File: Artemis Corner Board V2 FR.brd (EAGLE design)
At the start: 132.4 x 63.1 mm, 68 parts, among them U1 TPS562219, U2 TM4C1231C3PM, U21 LM1085IS, U3 TPS562219, U4 MCP2562FD, Y1 NX3225GA

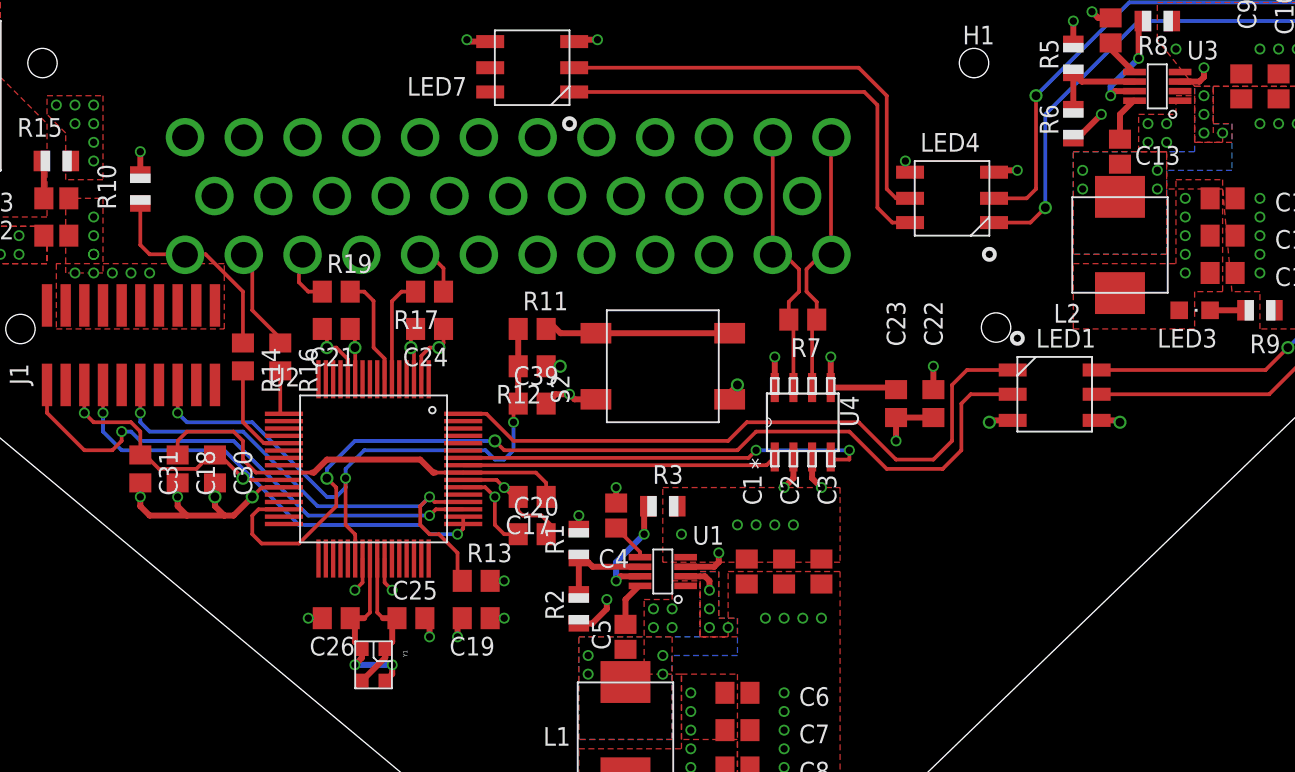
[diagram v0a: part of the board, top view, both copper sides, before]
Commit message: fixed board errors and added ESD Protection
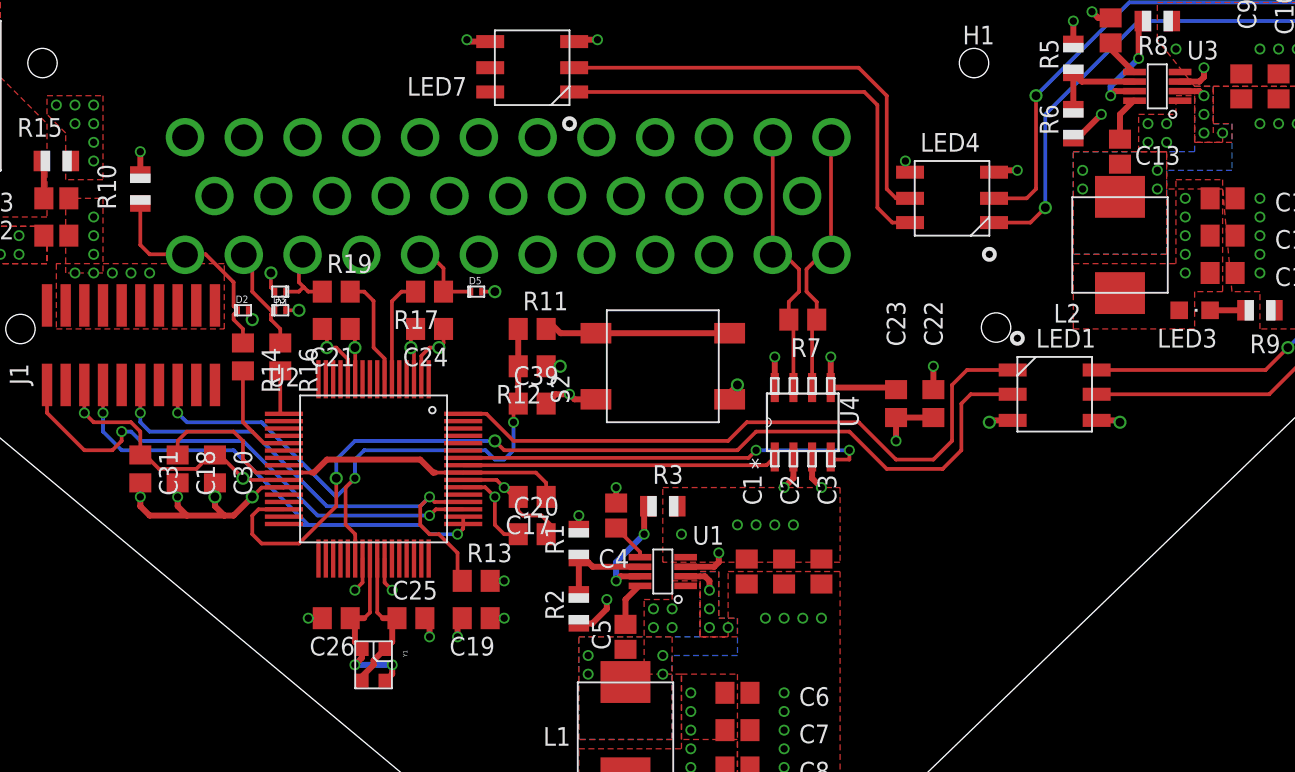
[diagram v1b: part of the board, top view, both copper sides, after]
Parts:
- added D2, D3, D4, D5: TPD1E05U06, FormE:X2SON
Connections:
- net DAMPER_POS_OUT: now also D3.I/O
- net GND: now also D2.GND, D3.GND, D4.GND, D5.GND
- net STRAIN_GADGE_VOLTMETER_IN_0: now also D5.I/O
- net STRAIN_GADGE_VOLTMETER_IN_1: now also D4.I/O
- net WHEEL_SPEED_OUT: now also D2.I/O
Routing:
- net GND: track 71.7 -> 75.7 mm, vias 67 -> 70
- net STRAIN_GADGE_VOLTMETER_IN_0: track 3.59 -> 5.47 mm
- net SW_5V2: track 0.00 -> 1.75 mm
- net STRAIN_GADGE_VOLTMETER_IN_1: track 3.83 -> 5.20 mm
- net TDO: track 31.6 -> 32.2 mm
- net SPI_SCARY_LED_CLOCK: track 66.7 -> 66.2 mm

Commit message: Made list fixes
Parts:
- moved D5 0.63 mm to (7.62, -5.08)
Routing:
- net STRAIN_GADGE_VOLTMETER_IN_0: track 5.47 -> 6.10 mm

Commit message: Updated a lot of stuff
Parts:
- added C62: 4.7uF, rcl:C0805
- added C63: 0.1uF, rcl:C0805
- added FB3: 220R @ 100M, launchpad:0805
- added R20: 2K, rcl:R0805
- C31: value 20uF -> 22uF
- turned C19 to 0 degrees
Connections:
- net P$40 renamed VDDC
- net PROGRAMMING_CAN_N renamed CAN_N
- net PROGRAMMING_CAN_P renamed CAN_P
- net PROGRAMMING_CAN_RX renamed CAN_RX
- net PROGRAMMING_CAN_TX renamed CAN_TX
- new net FILTERED_+3V3: C19.1, C20.1, C21.1, C24.1, C30.1, C31.1, C62.1, C63.1, FB3.2, U2.11, U2.2, U2.26, U2.42, U2.54
- new net N$7: R20.2, U2.41
- net +3V3: now also FB3.1; no longer C19.1, C20.1, C21.1, C24.1, C30.1, C31.1, U2.11, U2.2, U2.26, U2.42, U2.54
- net GND: now also C62.2, C63.2, U2.32, U2.35
- net N$5: now also R20.1; no longer U2.41
- net TDI: now also U2.50
- net TDO: no longer U2.50
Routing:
- net FILTERED_+3V3: track 0.00 -> 34.4 mm, vias 0 -> 6
- net +3V3: track 46.1 -> 14.7 mm, vias 15 -> 9
- net CAN_TX: track 21.7 -> 1.05 mm
- net CAN_RX: track 28.5 -> 9.06 mm
- net N$6: track 12.6 -> 16.6 mm
- net CAN_P: track 18.7 -> 17.5 mm
- net CAN_N: track 18.6 -> 17.3 mm
- net N$5: track 10.3 -> 9.42 mm
- net TDO: track 32.2 -> 31.7 mm

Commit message: Changed to Tiva C with two CAN modules; modified sensor input scaling
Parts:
- removed C62: 4.7uF, rcl:C0805
- removed C63: 0.1uF, rcl:C0805
- removed C72, C73: 10uF, adafruit:C0805
- removed D4, D5: TPD1E05U06, FormE:X2SON
- removed FB3: 220R @ 100M, launchpad:0805
- removed LED5, LED6: GREEN, FormE:CHIPLED_0805
- removed LED7: APA102C, FormE:5050_LED
- removed S2: TE-FSM4JSMATR, FormE:TE-FSM4JSMATR
- removed U21: LM1085IS, FormE:TO-263
- added C27, C33, C34, C35: 0.1uF, rcl:C0805
- added C28: 0.01uF, rcl:C0805
- added C29: 1uF, rcl:C0805
- added C32: 4.7uF, rcl:C0805
- added C36, C42: 0.1uF, adafruit:C0805
- added C37, C38: 10uF, adafruit:C0805
- added C40: 2.2uF, rcl:C0805
- added C41: 8200pF, adafruit:C0805
- added C43, C44: 22uF, rcl:C1210K
- added C45, C46, C47: 22uF, adafruit:C0805
- added CF1, CF2, CF3, CF4: NFM21C, murata-filter:NFM21C
- added D1: TPD1E05U06, FormE:X2SON
- added IC1: FT232RL, ftdichip:SSOP28
- added JP1: (no value), pinhead:1X02
- added JP2: (no value), FormE:MOLEX-MICROUSB-B-105017-0001
- added L3: 4.7uH, FormE:SRP6540
- added Q1: BSS138, FormE:BSS138
- added R21: 1k, adafruit:R0805
- added R22: 54.9k, adafruit:R0805
- added R23: 10K, adafruit:R0805
- added R24: 1K, adafruit:R0805
- added S1: TE-FSM4JSMATR, FormE:TE-FSM4JSMATR
- added U5: MCP2562, FormE:SOIC8-N_MC
- added U6: TPS62177, FormE:TPS6217X
- added U7: TPS62175, FormE:TPS6217X
- added U8: TPS562219, FormE:TPS562219
- added Y2: 32.768kHz, FormE:AB26TRQ
- C1: value 0.1uF -> 100uF; device adafruit:C0805 -> rcl:D/7343-31W
- C10, C2: value 10uF -> 0.1uF; device adafruit:C0805 -> rcl:C0805
- C11: value 10uF -> 2.2uF; device adafruit:C0805 -> rcl:C0805
- C12: value 8200pF -> 2.2uF; device adafruit:C0805 -> rcl:C0805
- C13, C5: device adafruit:C0805 -> rcl:C0805
- C14, C16: value 22uF -> 0.1uF; device adafruit:C0805 -> rcl:C0805
- C15: value 22uF -> DNP/0.1uF; device adafruit:C0805 -> rcl:C0805
- C18: value 3.3uF -> 22pF
- C19: value 0.1uF -> 1uF
- C20, C22, C23: value 0.1uF -> 22pF
- C21: value 0.1uF -> 2.2uF
- C24: value 0.1uF -> 0.01uF
- C25: value 12pF -> 0.1uF
- C26: value 12pF -> 0.01uF
- C3: value 10uF -> 100pF; device adafruit:C0805 -> rcl:C0805
- C31: value 22uF -> 0.1uF
- C39: value 1uF -> 2.2uF
- C4: value 8200pF -> 100pF; device adafruit:C0805 -> rcl:C0805
- C6, C7, C8: value 22uF -> 2.2uF; device adafruit:C0805 -> rcl:C0805
- C9: value 0.1uF -> DNP; device adafruit:C0805 -> rcl:C0805
- D3: value TPD1E05U06 -> MM3Z3V3T1G; device FormE:X2SON -> FormE:SOD-323
- L1, L2: value 4.7uH -> 10uH
- LED1, LED2: value APA102C -> ORANGE; device FormE:5050_LED -> FormE:CHIP-LED0805
- LED3: device FormE:CHIPLED_0805 -> FormE:CHIP-LED0805
- LED4: value APA102C -> GREEN; device FormE:5050_LED -> FormE:CHIP-LED0805
- R1: value 33.2K -> 100R; device adafruit:R0805 -> rcl:R0805
- R10: value 10K -> 270; device adafruit:R0805 -> rcl:R0805
- R11: value 100 -> 120R
- R12: value 2.2K -> 100R
- R13: value 1K -> 10k
- R14: value 22 -> 120R
- R15: value 0.007 -> 270; device adafruit:R0805 -> rcl:R0805
- R16: value 22 -> 270
- R17: value 22 -> 10k
- R18: value 1K -> 4.7k; device adafruit:R0805 -> rcl:R0805
- R19: value 22 -> 75k
- R2: value 10K -> 100R; device adafruit:R0805 -> rcl:R0805
- R20: value 2K -> 150k
- R3: value 10K -> 22; device adafruit:R0805 -> rcl:R0805
- R4: value 1K -> 22; device adafruit:R0805 -> rcl:R0805
- R5: value 33.2K -> 10k; device adafruit:R0805 -> rcl:R0805
- R6: value 10K -> 10k; device adafruit:R0805 -> rcl:R0805
- R7: value 120/DNP -> 10k
- R8: value 10K -> 39k; device adafruit:R0805 -> rcl:R0805
- R9: value 1K -> 75k; device adafruit:R0805 -> rcl:R0805
- U1: value TPS562219 -> OPA365AIDBVR; device FormE:TPS562219 -> FormE:SOT23-5
- U2: value TM4C1231C3PM -> ADS1232IPWR; device FormE:TM4C1231C3PM -> FormE:ADS1232IPW
- U3: value TPS562219 -> MCP2562; device FormE:TPS562219 -> FormE:SOIC8-N_MC
- U4: value MCP2562FD -> TM4C123GH6PMI; device FormE:SOIC8-N_MC -> FormE:PQFP-64
- Y1: value NX3225GA -> 16MHz; device FormE:4-SMD -> FormE:CSM-3X
- moved C23 467.3 mm to (-108.6, -457.2), turned to 0 degrees
- moved C22 462.1 mm to (-108.6, -450.9), turned to 0 degrees
- moved R7 451.0 mm to (-96.5, -440.1), turned to 0 degrees
- moved U1 435.3 mm to (-106.7, -440.7), turned to 0 degrees
- moved C1 412.4 mm to (-93.3, -419.1), turned to 0 degrees
- moved C4 407.2 mm to (-96.5, -411.5), turned to 0 degrees
- moved C3 401.6 mm to (-96.5, -405.1), turned to 0 degrees
- moved C2 394.8 mm to (-96.5, -398.8), turned to 0 degrees
- moved C10 381.1 mm to (-96.5, -337.8), turned to 0 degrees
- moved C12 374.1 mm to (-96.5, -331.5), turned to 0 degrees
- moved C11 370.6 mm to (-96.5, -325.1), turned to 0 degrees
- moved C7 363.1 mm to (-96.5, -377.2)
- moved C8 354.8 mm to (-96.5, -370.8)
- moved C6 353.6 mm to (-96.5, -364.5)
- moved R2 349.4 mm to (-96.5, -358.1), turned to 0 degrees
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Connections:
- removed net +12V: H1.1, H1.2, H1.3, LED6.A, R10.2, R15.2
- removed net 12V_CURRENT_SENSE+: C73.1, R15.1, U21.2, U21.GND, U21.GND1
- removed net CAN_N: H1.12, H1.35, R7.1, U4.6
- removed net CAN_P: H1.11, H1.34, R7.2, U4.7
- removed net CAN_RX: U2.58, U4.4
- removed net CAN_TX: U2.57, U4.1
- removed net DAMPER_POS_OUT: D3.I/O, H1.25, R16.1
- removed net DAMPER_POS_OUT_TR: R16.2, U2.17
- removed net FILTERED_+3V3: C19.1, C20.1, C21.1, C24.1, C30.1, C31.1, C62.1, C63.1, FB3.2, U2.11, U2.2, U2.26, U2.42, U2.54
- removed net MCU_RESET: C39.1, J1.15, R11.1, R12.2, U2.38
- removed net N$11: LED6.C, R18.2
- removed net SPI_SCARY_LED_CLOCK: LED1.2, U2.30
- removed net SPI_SCARY_LED_TRANSMIT: LED1.1, U2.64
- removed net SS_5V1: C4.1, U1.5
- removed net SS_5V2: C12.1, U3.5
- removed net STRAIN_GADGE_VOLTMETER_IN_0: D5.I/O, H1.28, R17.1
- removed net STRAIN_GADGE_VOLTMETER_IN_0_TR: R17.2, U2.6
- removed net STRAIN_GADGE_VOLTMETER_IN_1: D4.I/O, H1.26, R19.1
- removed net STRAIN_GADGE_VOLTMETER_IN_1_TR: R19.2, U2.7
- removed net SW_5V1: C5.2, L1.P$1, U1.2
- removed net SW_5V2: C13.2, L2.P$1, U3.2
- removed net TRCLK: U2.31
- removed net VBST_5V1: C5.1, U1.8
- removed net VBST_5V2: C13.1, U3.8
- removed net VDDC: C17.1, C18.1, U2.25, U2.56
- removed net VFB_5V1: R1.1, R2.2, U1.6
- removed net VFB_5V2: R5.1, R6.2, U3.6
- removed net WHEEL_SPEED_OUT: D2.I/O, H1.24, R10.1, R14.1
- removed net WHEEL_SPEED_OUT_TR: R14.2, U2.21
- new net !RESET!: C15.1, J1.15, R12.2, R13.2, U4.38
- new net +1V2: C44.1, L2.P$2, R19.2, U7.10, U7.8, U7.MASK-10, U7.MASK-8
- new net ADC_!PWDN!: U2.22, U4.46
- new net ADC_CHANNEL_SELECT: U2.8, U4.48
- new net ADC_GAIN_BIT_0: U2.19, U4.58
- new net ADC_GAIN_BIT_1: U2.20, U4.57
- new net ADC_MISO: U2.24, U4.21
- new net ADC_SCLK: U2.23, U4.19
- new net ADC_SPEED: U2.21, U4.45
- new net ADC_TEMP_EN: U2.7, U4.47
- new net CAR_CAN_N: H1.35, R14.1, U5.6
- new net CAR_CAN_P: H1.34, R14.2, U5.7
- new net CAR_CAN_RX: U4.59, U5.4
- new net CAR_CAN_TX: U4.60, U5.1
- new net DAMPER_POSITION: D1.I/O, H1.25, R3.1
- new net DAMPER_POSITION_3V3: D3.CATHODE, R10.2, U4.6
- new net FB_1V2: R19.1, R20.2, U7.5, U7.MASK-5
- new net IR_SENSOR_CAN_N: H1.12, R11.1, U3.6
- new net IR_SENSOR_CAN_P: H1.11, R11.2, U3.7
- new net N$14: R8.2, U1.1, U1.4
- new net N$17: C23.1, U4.34, Y2.1
- new net N$19: JP1.2, U2.14
- new net N$20: R3.2, R5.1, U1.3
- new net N$21: Q1.D, R4.2, R6.1
- new net N$22: C35.1, IC1.17
- new net N$23: JP2.1, JP2.P$1, R18.1
- new net N$24: C22.2, C23.2, U4.35
- new net N$27: C2.1, C3.1, CF1.3, U2.11
- new net N$29: C2.2, C4.1, CF2.1, U2.12
- new net N$41: IC1.22, R16.1
- new net N$42: IC1.23, R15.1
- new net N$45: LED1.C, R15.2
- new net N$46: LED2.C, R16.2
- new net N$52: IC1.19, R17.1, R18.2
- new net N$8: C10.2, U2.9
- new net NTRST: J1.2
- new net PGOOD: U6.7, U6.MASK-7, U7.7, U7.MASK-7, U8.4
- new net RTCK: J1.9
- new net SENSOR_CAN_RX: U3.4, U4.17
- new net SENSOR_CAN_TX: U3.1, U4.18
- new net SS_5V: C41.1, U8.5
- new net STRAIN_GAUGE_NEGATIVE: CF2.3, H1.26
- new net STRAIN_GAUGE_POSITIVE: CF1.1, H1.28
- new net SW_1V2: L2.P$1, U7.9, U7.MASK-9
- new net SW_3V3: L1.P$1, U6.9, U6.MASK-9
- new net SW_5V: C42.2, L3.P$1, U8.2
- new net UART_RX: IC1.1, U4.16
- new net UART_TX: IC1.5, U4.15
- new net USB_D_N: IC1.16, JP2.2, JP2.P$2
- new net USB_D_P: IC1.15, JP2.3, JP2.P$3
- new net VBST_5V: C42.1, U8.8
- new net VFB_5V: R22.1, R23.2, U8.6
- new net WHEEL_TACHOMETER: D2.I/O, H1.24, R4.1
- new net WHEEL_TACHOMETER_3V3: Q1.S, R7.1, U4.1
- net +3V3: now also C12.1, C13.1, C24.1, C25.1, C26.1, C27.1, C28.1, C29.1, C31.1, C34.1, C43.1, IC1.4, LED1.A, LED2.A, LED3.A, Q1.G, R13.1, R7.2, U2.1, U3.5, U4.11, U4.2, U4.26, U4.37, U4.42, U4.54, U5.5, U6.10, U6.8, U6.MASK-10, U6.MASK-8; no longer C23.1, C6.1, C7.1, C8.1, FB3.1, LED5.A, R1.2, R12.1, U4.5
- net +5V: now also C11.1, C30.1, C32.1, C33.1, C45.1, C46.1, C47.1, C5.1, IC1.20, L3.P$2, LED4.A, R1.1, R22.2, R6.2, U1.5, U2.18, U3.3, U5.3; no longer C15.1, C16.1, C22.1, H1.10, L2.P$2, LED1.4, LED2.4, LED3.A, LED4.4, LED7.4, R5.2, U4.3
- net GND: now also C13.2, C27.2, C28.2, C29.2, C32.2, C33.2, C34.2, C35.2, C36.2, C37.2, C38.2, C40.2, C41.2, C43.2, C44.2, C45.2, C46.2, C47.2, C5.2, CF1.2@1, CF2.2@1, CF3.2@1, CF4.2@1, D1.GND, D3.ANODE, IC1.18, IC1.21, IC1.25, IC1.26, IC1.7, JP2.5, JP2.P$5, JP2.P$6, JP2.P$7, JP2.P$8, JP2.P$9, R17.2, R20.1, R21.1, R23.1, R24.1, R5.2, S1.3, S1.4, U1.2, U2.17, U2.2, U2.5, U2.6, U3.2, U3.8, U4.12, U4.27, U4.3, U4.32, U4.39, U4.55, U5.2, U5.8, U6.1, U6.4, U6.5, U6.6, U6.MASK-1, U6.MASK-4, U6.MASK-5, U6.MASK-6, U6.PAD, U6.PAD-HOLE-1, U6.PAD-HOLE-2, U6.PAD-HOLE-3, U6.PAD1, U6.PAD2, U7.1, U7.4, U7.6, U7.MASK-1, U7.MASK-4, U7.MASK-6, U7.PAD, U7.PAD-HOLE-1, U7.PAD-HOLE-2, U7.PAD-HOLE-3, U7.PAD1, U7.PAD2, U8.1; no longer C1.2, C10.2, C2.2, C22.2, C23.2, C6.2, C62.2, C63.2, C72.2, C73.2, D3.GND, D4.GND, D5.GND, H1.19, H1.20, H1.21, H1.22, H1.23, LED1.3, LED2.3, LED4.3, LED7.3, R13.2, R18.1, R4.1, R6.1, S2.3, S2.4, U1.1, U2.12, U2.27, U2.32, U2.35, U2.39, U2.55, U21.1, U3.1, U4.2, U4.8
- net N$1: now also C18.1, U4.41, Y1.P$1; no longer LED1.6, LED2.1
- net N$10: now also C6.1, C7.1, CF3.3, U2.16; no longer LED2.6, LED4.1
- net N$12: now also C6.2, C8.1, CF4.1, U2.15; no longer LED4.5, LED7.2
- net N$13: now also C1.+, CF3.1, R1.2; no longer LED4.6, LED7.1
- net N$15: now also C22.1, U4.36, Y2.2; no longer LED2.5, LED4.2
- net N$16: now also C9.1, R10.1, R8.1, R9.2; no longer LED1.5, LED2.2
- net N$18: now also C1.-, CF4.3, R2.2; no longer R11.2, S2.1, S2.2
- net N$2: now also LED3.C, R21.2; no longer LED5.C, R4.2
- net N$3: now also LED4.C, R24.2; no longer LED3.C, R9.2
- net N$4: now also C20.1, U4.40, Y1.P$2; no longer R8.2, U3.7
- net N$5: now also C10.1, U2.10; no longer C25.1, R20.1, Y1.1, Y1.3
- net N$6: now also C16.1, C17.1, C19.1, C21.1, U4.25, U4.56; no longer C26.1, U2.40, Y1.2, Y1.4
- net N$7: now also R12.1, S1.1, S1.2; no longer R20.2, U2.41
- net N$9: now also JP1.1, U2.13; no longer R3.2, U1.7
- net TCK: now also U4.52; no longer R13.1, U2.52
- net TDI: now also U4.50; no longer U2.50
- net TDO: now also U4.49; no longer U2.49
- net TMS: now also U4.51; no longer U2.51
- net VCC: now also C36.1, C37.1, C38.1, C39.1, C40.1, U6.2, U6.3, U6.MASK-2, U6.MASK-3, U7.2, U7.3, U7.MASK-2, U7.MASK-3, U8.3, U8.7; no longer C1.1, C10.1, C11.1, C2.1, C3.1, C72.1, C9.1, H1.32, R3.1, R8.1, U1.3, U21.3, U3.3
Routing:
- net GND: track 75.3 -> 0.00 mm, vias 70 -> 0
- net SPI_SCARY_LED_CLOCK: track 66.2 -> 0.00 mm, vias 2 -> 0
- net SPI_SCARY_LED_TRANSMIT: track 44.5 -> 0.00 mm
- net MCU_RESET: track 44.1 -> 0.00 mm, vias 3 -> 0
- net N$15: track 40.2 -> 0.00 mm, vias 2 -> 0
- net N$10: track 37.7 -> 0.00 mm, vias 2 -> 0
- net TCK: track 34.8 -> 0.00 mm, vias 2 -> 0
- net TMS: track 34.7 -> 0.00 mm, vias 2 -> 0
- net FILTERED_+3V3: track 34.4 -> 0.00 mm, vias 6 -> 0
- net N$16: track 34.1 -> 0.00 mm, vias 2 -> 0
- net N$1: track 31.9 -> 0.00 mm, vias 2 -> 0
- net TDO: track 31.7 -> 0.00 mm, vias 2 -> 0
- net N$13: track 30.6 -> 0.00 mm
- net N$12: track 30.3 -> 0.00 mm
- net VDDC: track 30.2 -> 0.00 mm
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- removed copper zone on layer 1, net +12V
- removed copper zone on layer 1, net +3V3
- removed copper zone on layer 1, net +5V
- removed copper zone on layer 1, net 12V_CURRENT_SENSE+
- removed copper zone on layer 1, net GND
- removed copper zone on layer 1, net SW_5V1
- removed copper zone on layer 16, net SW_5V1
- removed copper zone on layer 1, net SW_5V2
- removed copper zone on layer 16, net SW_5V2
- removed copper zone on layer 1, net VCC

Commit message: Grouped components in layout
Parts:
- moved C23 407.9 mm to (128.3, -125.1)
- moved C22 404.8 mm to (128.3, -122.6)
- moved Y2 404.8 mm to (130.8, -118.1)
- moved U4 263.4 mm to (142.2, -101.6), turned to 45 degrees
- moved C29 258.1 mm to (113.7, -88.3), turned to 225 degrees
- moved R3 249.2 mm to (-73.7, -320.0)
- moved D1 240.8 mm to (-74.9, -322.6)
- moved U8 216.6 mm to (144.1, -212.7)
- moved R12 206.7 mm to (83.8, -143.5)
- moved R4 193.6 mm to (-92.1, -262.3)
- moved R7 188.6 mm to (-92.1, -251.5)
- moved D2 185.3 mm to (-92.1, -264.8)
- moved Q1 178.4 mm to (-92.1, -255.3)
- moved JP1 156.6 mm to (-4.45, -299.1)
- moved C1 151.4 mm to (-14.0, -290.2)
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- renumbered IC1 to U9

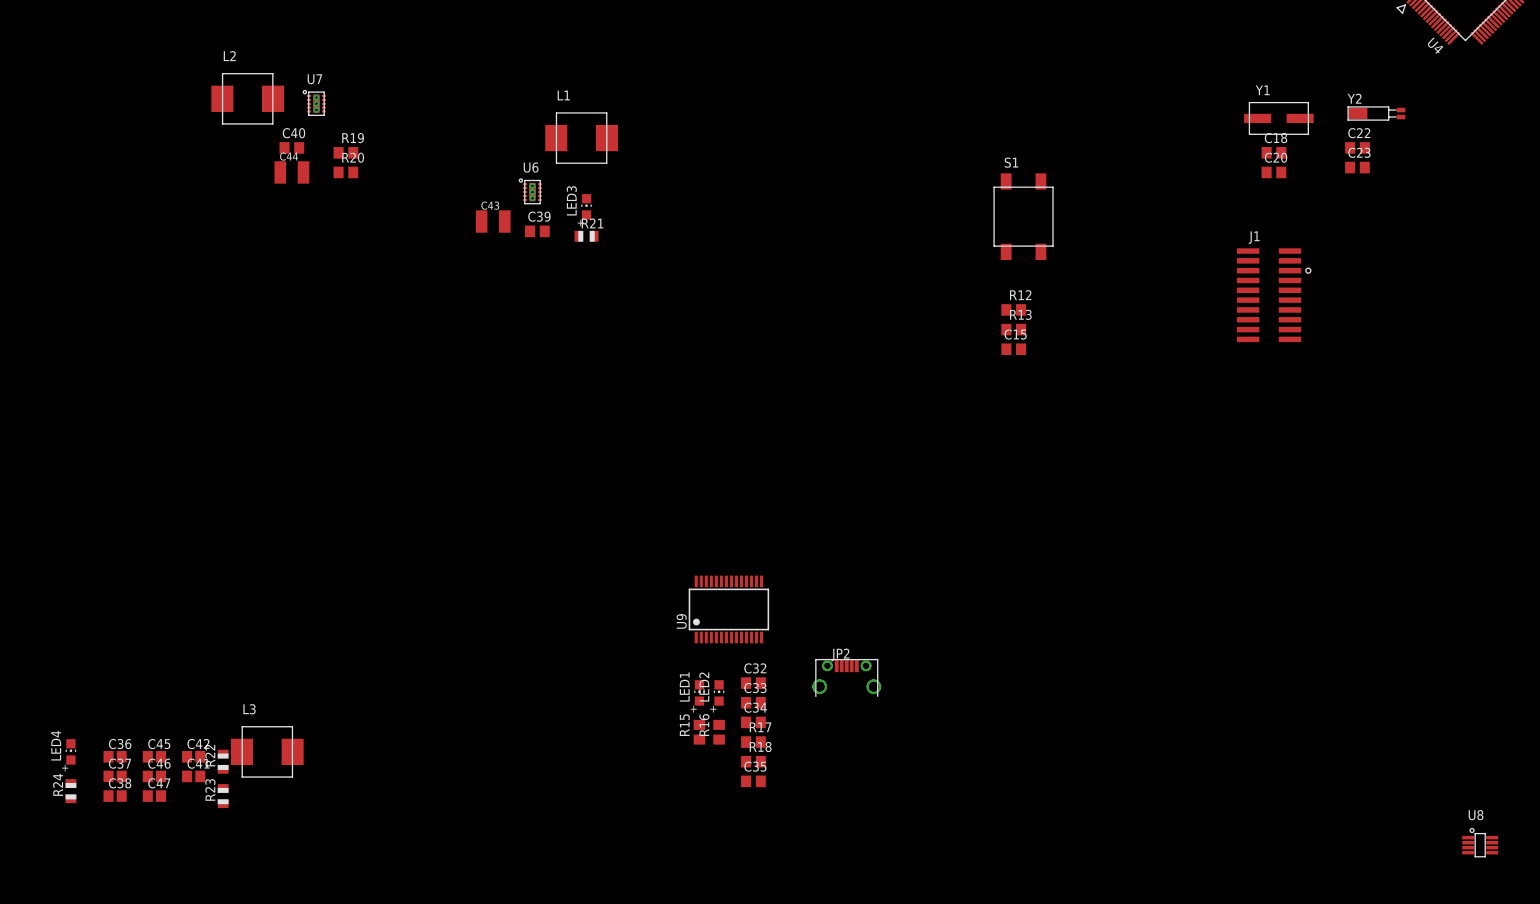
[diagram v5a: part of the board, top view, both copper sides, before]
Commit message: Changed to smaller LM3671 regulators
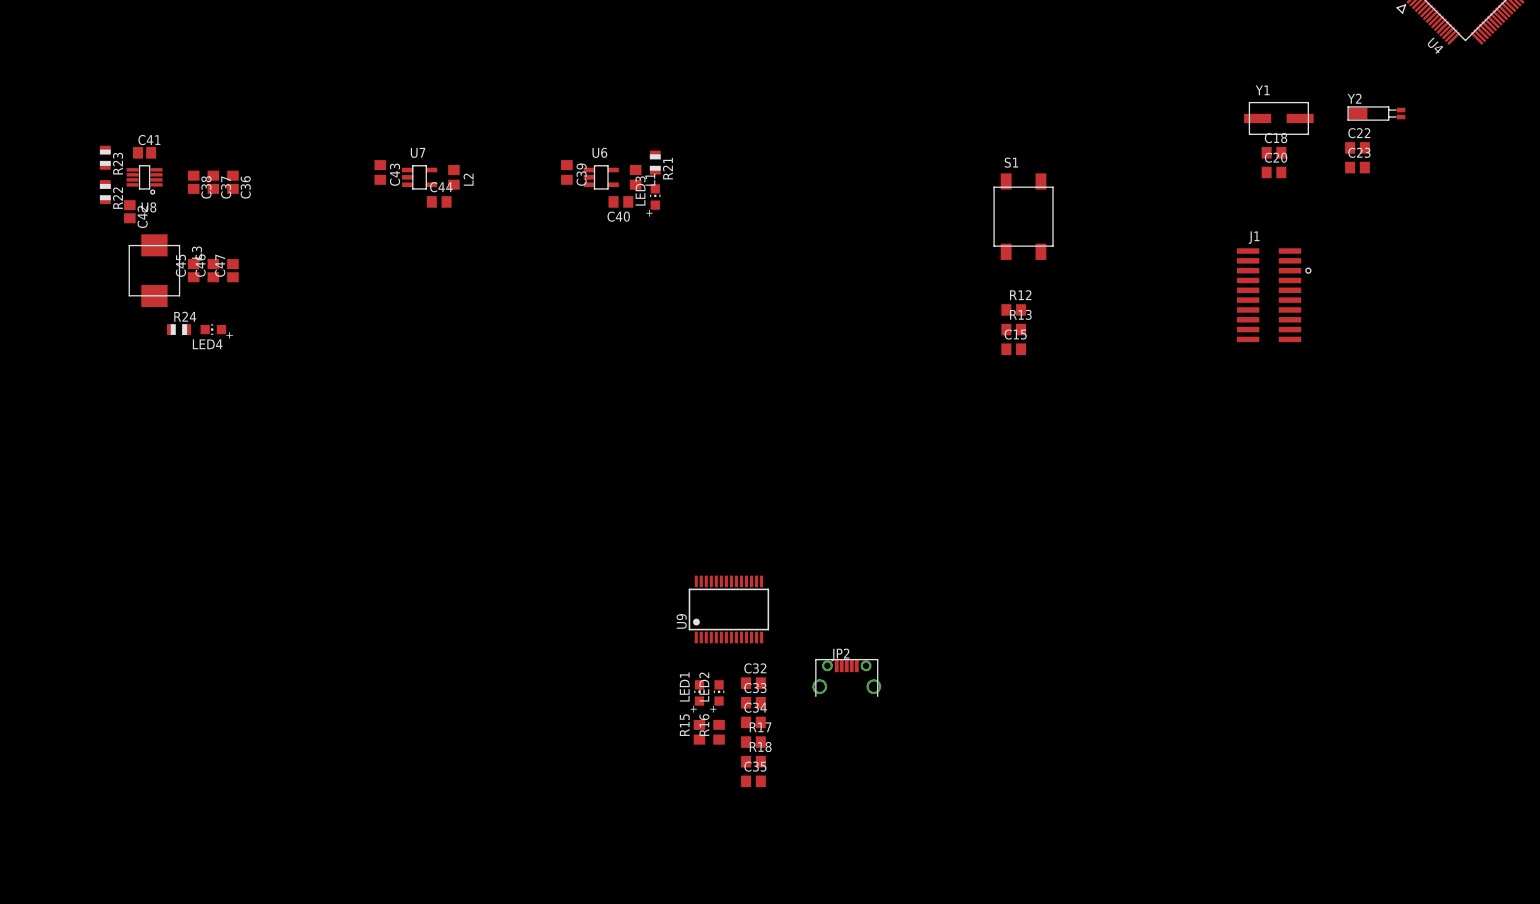
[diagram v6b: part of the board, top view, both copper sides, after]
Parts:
- removed R19: 75k, rcl:R0805
- removed R20: 150k, rcl:R0805
- C39: value 2.2uF -> 4.7uF
- C40: value 2.2uF -> 10uF
- C43: value 22uF -> 4.7uF; device rcl:C1210K -> rcl:C0805
- C44: value 22uF -> 10uF; device rcl:C1210K -> rcl:C0805
- L1, L2: value 10uH -> (none); device FormE:SRP6540 -> FormE:0805
- U6: value TPS62177 -> LM3671MF-3.3/NOPB; device FormE:TPS6217X -> FormE:SOT23-5
- U7: value TPS62175 -> LM3671MF-1.2/NOPB; device FormE:TPS6217X -> FormE:SOT23-5
- moved U8 193.1 mm to (-28.6, -126.4), turned to 180 degrees
- moved R23 83.9 mm to (-33.7, -123.8), turned to 270 degrees
- moved C41 80.9 mm to (-28.6, -123.2)
- moved C38 80.0 mm to (-22.2, -127.0), turned to 270 degrees
- moved C37 77.9 mm to (-19.7, -127.0), turned to 270 degrees
- moved C36 75.8 mm to (-17.1, -127.0), turned to 270 degrees
- moved R22 75.2 mm to (-33.7, -128.3), turned to 270 degrees
- moved C42 71.0 mm to (-30.5, -130.8), turned to 270 degrees
- moved C47 68.7 mm to (-17.1, -138.4), turned to 90 degrees
- moved C46 65.8 mm to (-19.7, -138.4), turned to 90 degrees
- moved L3 63.9 mm to (-27.3, -138.4), turned to 270 degrees
- moved C45 63.1 mm to (-22.2, -138.4), turned to 90 degrees
- moved R24 61.3 mm to (-24.1, -146.1), turned to 0 degrees
- moved LED4 57.6 mm to (-19.7, -146.1), turned to 90 degrees
- moved C40 43.1 mm to (33.0, -129.5), turned to 180 degrees
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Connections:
- removed net FB_1V2: R19.1, R20.2, U7.5, U7.MASK-5
- removed net SW_1V2: L2.P$1, U7.9, U7.MASK-9
- removed net SW_3V3: L1.P$1, U6.9, U6.MASK-9
- new net N$11: L1.1, U6.5
- new net N$25: L2.1, U7.5
- net +1V2: now also L2.2, U7.4; no longer L2.P$2, R19.2, U7.10, U7.8, U7.MASK-10, U7.MASK-8
- net +3V3: now also C40.1, L1.2, U6.4; no longer C43.1, L1.P$2, U6.10, U6.8, U6.MASK-10, U6.MASK-8
- net +5V: now also C39.1, C43.1, U6.1, U6.3, U7.1, U7.3
- net GND: now also U6.2, U7.2; no longer R20.1, U6.1, U6.4, U6.5, U6.6, U6.MASK-1, U6.MASK-4, U6.MASK-5, U6.MASK-6, U6.PAD, U6.PAD-HOLE-1, U6.PAD-HOLE-2, U6.PAD-HOLE-3, U6.PAD1, U6.PAD2, U7.1, U7.4, U7.6, U7.MASK-1, U7.MASK-4, U7.MASK-6, U7.PAD, U7.PAD-HOLE-1, U7.PAD-HOLE-2, U7.PAD-HOLE-3, U7.PAD1, U7.PAD2
- net PGOOD: no longer U6.7, U6.MASK-7, U7.7, U7.MASK-7
- net VCC: no longer C39.1, C40.1, U6.2, U6.3, U6.MASK-2, U6.MASK-3, U7.2, U7.3, U7.MASK-2, U7.MASK-3
